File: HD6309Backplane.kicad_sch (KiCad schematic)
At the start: 8 parts, among them J1 Conn_01x02_Female, J2 Conn_02x30_Odd_Even, J3 Conn_01x02_Female, J4 Conn_01x02_Female, J5 Conn_01x02_Female, J6 Conn_02x30_Odd_Even, J7 Conn_02x30_Odd_Even, J8 Conn_02x30_Odd_Even

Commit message: align to new expansion position
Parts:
- added J10: Power probe, Connector_PinSocket_2.54mm:PinSocket_1x02_P2.54mm_Vertical, symbol Connector:Conn_01x02_Female
- added J9: External power, Connector_PinSocket_2.54mm:PinSocket_1x02_P2.54mm_Vertical, symbol Connector:Conn_01x02_Female
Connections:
- net +5V: now also J10.1 (Pin_1), J9.1 (Pin_1)
- net GND: now also J10.2 (Pin_2), J9.2 (Pin_2)
- net Q8: now reaches J7.45 (Pin_45)
- net Q8: now also J2.45 (Pin_45), J6.45 (Pin_45), J8.45 (Pin_45)
- no-connect marks 36 -> 32
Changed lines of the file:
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@@
   (no_connect (at 39.116 156.21))
   (no_connect (at 26.416 143.51))
-  (no_connect (at 192.024 52.07))
-  (no_connect (at 36.576 143.51))
   (no_connect (at 27.178 96.266))
   (no_connect (at 29.718 47.498))
@@
   (no_connect (at 100.838 47.498))
   (no_connect (at 176.784 52.07))
-  (no_connect (at 44.958 47.498))
   (no_connect (at 60.198 96.266))
   (no_connect (at 59.436 143.51))
-  (no_connect (at 37.338 96.266))
   (no_connect (at 93.218 96.266))
   (no_connect (at 21.336 143.51))
@@
     )
   )
+  (global_label "Q8" (shape input) (at 36.576 143.51 90) (fields_autoplaced)
+    (effects (font (size 1.27 1.27)) (justify left))
+    (property "Intersheet References" "${INTERSHEET_REFS}" (id 0) (at 36.4966 138.5569 90)
+      (effects (font (size 1.27 1.27)) (justify left) hide)
+    )
+  )
+  (global_label "Q8" (shape input) (at 44.958 47.498 90) (fields_autoplaced)
+    (effects (font (size 1.27 1.27)) (justify left))
+    (property "Intersheet References" "${INTERSHEET_REFS}" (id 0) (at 44.8786 42.5449 90)
+      (effects (font (size 1.27 1.27)) (justify left) hide)
+    )
+  )
   (global_label "Clock24" (shape input) (at 90.678 96.266 90) (fields_autoplaced)
     (effects (font (size 1.27 1.27)) (justify left))
@@
     )
   )
+  (global_label "Q8" (shape input) (at 192.024 52.07 90) (fields_autoplaced)
+    (effects (font (size 1.27 1.27)) (justify left))
+    (property "Intersheet References" "${INTERSHEET_REFS}" (id 0) (at 191.9446 47.1169 90)
+      (effects (font (size 1.27 1.27)) (justify left) hide)
+    )
+  )
   (global_label "~{Q}" (shape input) (at 82.296 143.51 90) (fields_autoplaced)
     (effects (font (size 1.27 1.27)) (justify left))
@@
     (effects (font (size 1.27 1.27)) (justify left))
     (property "Intersheet References" "${INTERSHEET_REFS}" (id 0) (at 80.5974 42.6054 90)
+      (effects (font (size 1.27 1.27)) (justify left) hide)
+    )
+  )
+  (global_label "Q8" (shape input) (at 37.338 96.266 90) (fields_autoplaced)
+    (effects (font (size 1.27 1.27)) (justify left))
+    (property "Intersheet References" "${INTERSHEET_REFS}" (id 0) (at 37.2586 91.3129 90)
       (effects (font (size 1.27 1.27)) (justify left) hide)
     )
@@
     )
     (property "Datasheet" "" (id 3) (at 83.82 29.972 0)
+      (effects (font (size 1.27 1.27)) hide)
+    )
+    (pin "1")
+  )
+  (symbol (lib_id "power:+5V") (at 155.956 120.142 0) (unit 1)
+    (in_bom yes) (on_board yes) (fields_autoplaced)
+    (property "Reference" "#PWR019" (id 0) (at 155.956 123.952 0)
+      (effects (font (size 1.27 1.27)) hide)
+    )
+    (property "Value" "+5V" (id 1) (at 155.956 115.316 0))
+    (property "Footprint" "" (id 2) (at 155.956 120.142 0)
+      (effects (font (size 1.27 1.27)) hide)
+    )
+    (property "Datasheet" "" (id 3) (at 155.956 120.142 0)
       (effects (font (size 1.27 1.27)) hide)
     )
@@
     (pin "9")
   )
+  (symbol (lib_id "power:GND") (at 155.956 122.682 0) (unit 1)
+    (in_bom yes) (on_board yes) (fields_autoplaced)
+    (property "Reference" "#PWR020" (id 0) (at 155.956 129.032 0)
+      (effects (font (size 1.27 1.27)) hide)
+    )
+    (property "Value" "GND" (id 1) (at 155.956 127.254 0))
+    (property "Footprint" "" (id 2) (at 155.956 122.682 0)
+      (effects (font (size 1.27 1.27)) hide)
+    )
+    (property "Datasheet" "" (id 3) (at 155.956 122.682 0)
+      (effects (font (size 1.27 1.27)) hide)
+    )
+    (pin "1")
+  )
   (symbol (lib_id "Connector:Conn_01x02_Female") (at 242.57 31.496 0) (unit 1)
     (in_bom yes) (on_board yes) (fields_autoplaced)
@@
     (pin "2")
   )
+  (symbol (lib_id "power:+5V") (at 155.702 103.886 0) (unit 1)
+    (in_bom yes) (on_board yes) (fields_autoplaced)
+    (property "Reference" "#PWR016" (id 0) (at 155.702 107.696 0)
+      (effects (font (size 1.27 1.27)) hide)
+    )
+    (property "Value" "+5V" (id 1) (at 155.702 99.06 0))
+    (property "Footprint" "" (id 2) (at 155.702 103.886 0)
+      (effects (font (size 1.27 1.27)) hide)
+    )
+    (property "Datasheet" "" (id 3) (at 155.702 103.886 0)
+      (effects (font (size 1.27 1.27)) hide)
+    )
+    (pin "1")
+  )
   (symbol (lib_id "power:GND") (at 177.546 35.306 0) (unit 1)
     (in_bom yes) (on_board yes) (fields_autoplaced)
@@
     )
     (pin "1")
+  )
+  (symbol (lib_id "power:GND") (at 155.702 106.426 0) (unit 1)
+    (in_bom yes) (on_board yes) (fields_autoplaced)
+    (property "Reference" "#PWR017" (id 0) (at 155.702 112.776 0)
+      (effects (font (size 1.27 1.27)) hide)
+    )
+    (property "Value" "GND" (id 1) (at 155.702 110.998 0))
+    (property "Footprint" "" (id 2) (at 155.702 106.426 0)
+      (effects (font (size 1.27 1.27)) hide)
+    )
+    (property "Datasheet" "" (id 3) (at 155.702 106.426 0)
+      (effects (font (size 1.27 1.27)) hide)
+    )
+    (pin "1")
+  )
+  (symbol (lib_id "Connector:Conn_01x02_Female") (at 160.782 103.886 0) (unit 1)
+    (in_bom yes) (on_board yes) (fields_autoplaced)
+    (property "Reference" "J9" (id 0) (at 161.544 103.8859 0)
+      (effects (font (size 1.27 1.27)) (justify left))
+    )
+    (property "Value" "External power" (id 1) (at 161.544 106.4259 0)
+      (effects (font (size 1.27 1.27)) (justify left))
+    )
+    (property "Footprint" "Connector_PinSocket_2.54mm:PinSocket_1x02_P2.54mm_Vertical" (id 2) (at 160.782 103.886 0)
+      (effects (font (size 1.27 1.27)) hide)
+    )
+    (property "Datasheet" "~" (id 3) (at 160.782 103.886 0)
+      (effects (font (size 1.27 1.27)) hide)
+    )
+    (pin "1")
+    (pin "2")
   )
   (symbol (lib_id "Connector_Generic:Conn_02x30_Odd_Even") (at 56.896 148.59 270) (unit 1)
@@
     (pin "1")
   )
+  (symbol (lib_id "Connector:Conn_01x02_Female") (at 161.036 120.142 0) (unit 1)
+    (in_bom yes) (on_board yes) (fields_autoplaced)
+    (property "Reference" "J10" (id 0) (at 161.798 120.1419 0)
+      (effects (font (size 1.27 1.27)) (justify left))
+    )
+    (property "Value" "Power probe" (id 1) (at 161.798 122.6819 0)
+      (effects (font (size 1.27 1.27)) (justify left))
+    )
+    (property "Footprint" "Connector_PinSocket_2.54mm:PinSocket_1x02_P2.54mm_Vertical" (id 2) (at 161.036 120.142 0)
+      (effects (font (size 1.27 1.27)) hide)
+    )
+    (property "Datasheet" "~" (id 3) (at 161.036 120.142 0)
+      (effects (font (size 1.27 1.27)) hide)
+    )
+    (pin "1")
+    (pin "2")
+  )
   (symbol (lib_id "power:+5V") (at 83.82 27.432 0) (unit 1)
     (in_bom yes) (on_board yes) (fields_autoplaced)
@@
       (reference "#PWR015") (unit 1) (value "+5V") (footprint "")
     )
+    (path "/8b947d1a-ce20-4218-9a3c-63eecca4c075"
+      (reference "#PWR016") (unit 1) (value "+5V") (footprint "")
+    )
+    (path "/b3f889d3-c00c-4e39-8b1d-e37941cea040"
+      (reference "#PWR017") (unit 1) (value "GND") (footprint "")
+    )
     (path "/04b6a0a1-8ff0-4daa-918c-930663744d50"
       (reference "#PWR018") (unit 1) (value "+5V") (footprint "")
     )
+    (path "/2037523f-8ef9-4ff2-a248-01a9f31a3eb5"
+      (reference "#PWR019") (unit 1) (value "+5V") (footprint "")
+    )
+    (path "/825dee91-fb4b-4957-9524-3022f9b93baf"
+      (reference "#PWR020") (unit 1) (value "GND") (footprint "")
+    )
     (path "/3992ff7e-16e7-40cc-9fb3-3ae7d9eb5f3a"
       (reference "J1") (unit 1) (value "Conn_01x02_Female") (footprint "Connector_PinSocket_2.54mm:PinSocket_1x02_P2.54mm_Vertical")
@@
       (reference "J8") (unit 1) (value "Conn_02x30_Odd_Even") (footprint "Connector_PinSocket_2.54mm:PinSocket_2x30_P2.54mm_Vertical")
     )
-  )
+    (path "/bac68116-967b-4b60-a3ef-e7e9a8644fbb"
+      (reference "J9") (unit 1) (value "External power") (footprint "Connector_PinSocket_2.54mm:PinSocket_1x02_P2.54mm_Vertical")
+    )
+    (path "/da05af8c-bcc2-4152-b839-cc8e4505fae5"
+      (reference "J10") (unit 1) (value "Power probe") (footprint "Connector_PinSocket_2.54mm:PinSocket_1x02_P2.54mm_Vertical")
+    )
+  )

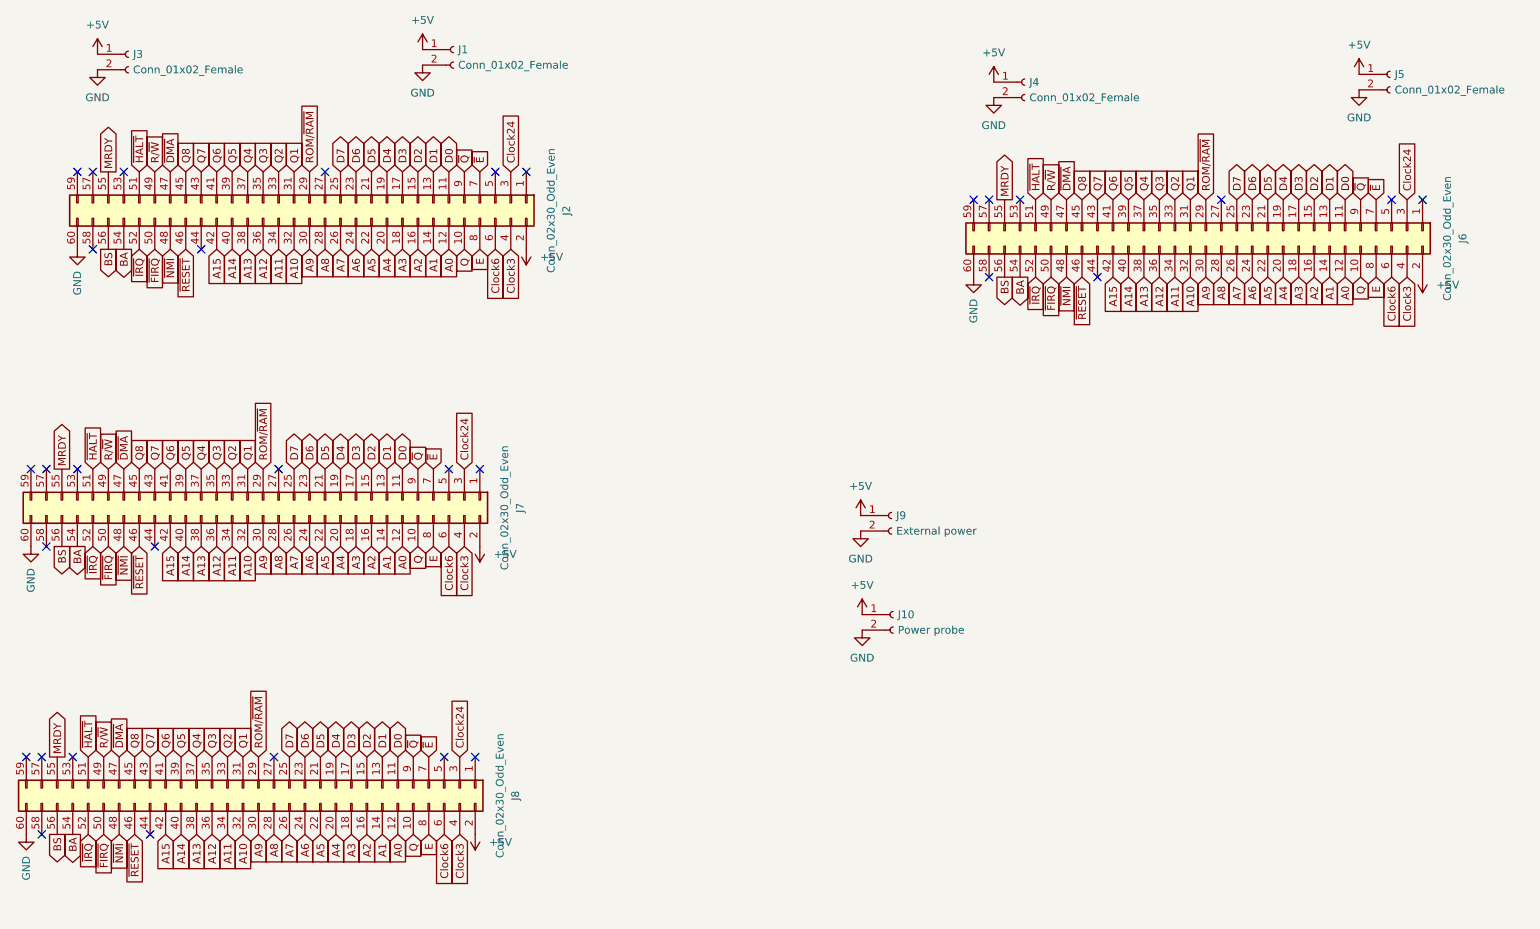
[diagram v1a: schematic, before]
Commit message: add mapped memory lane
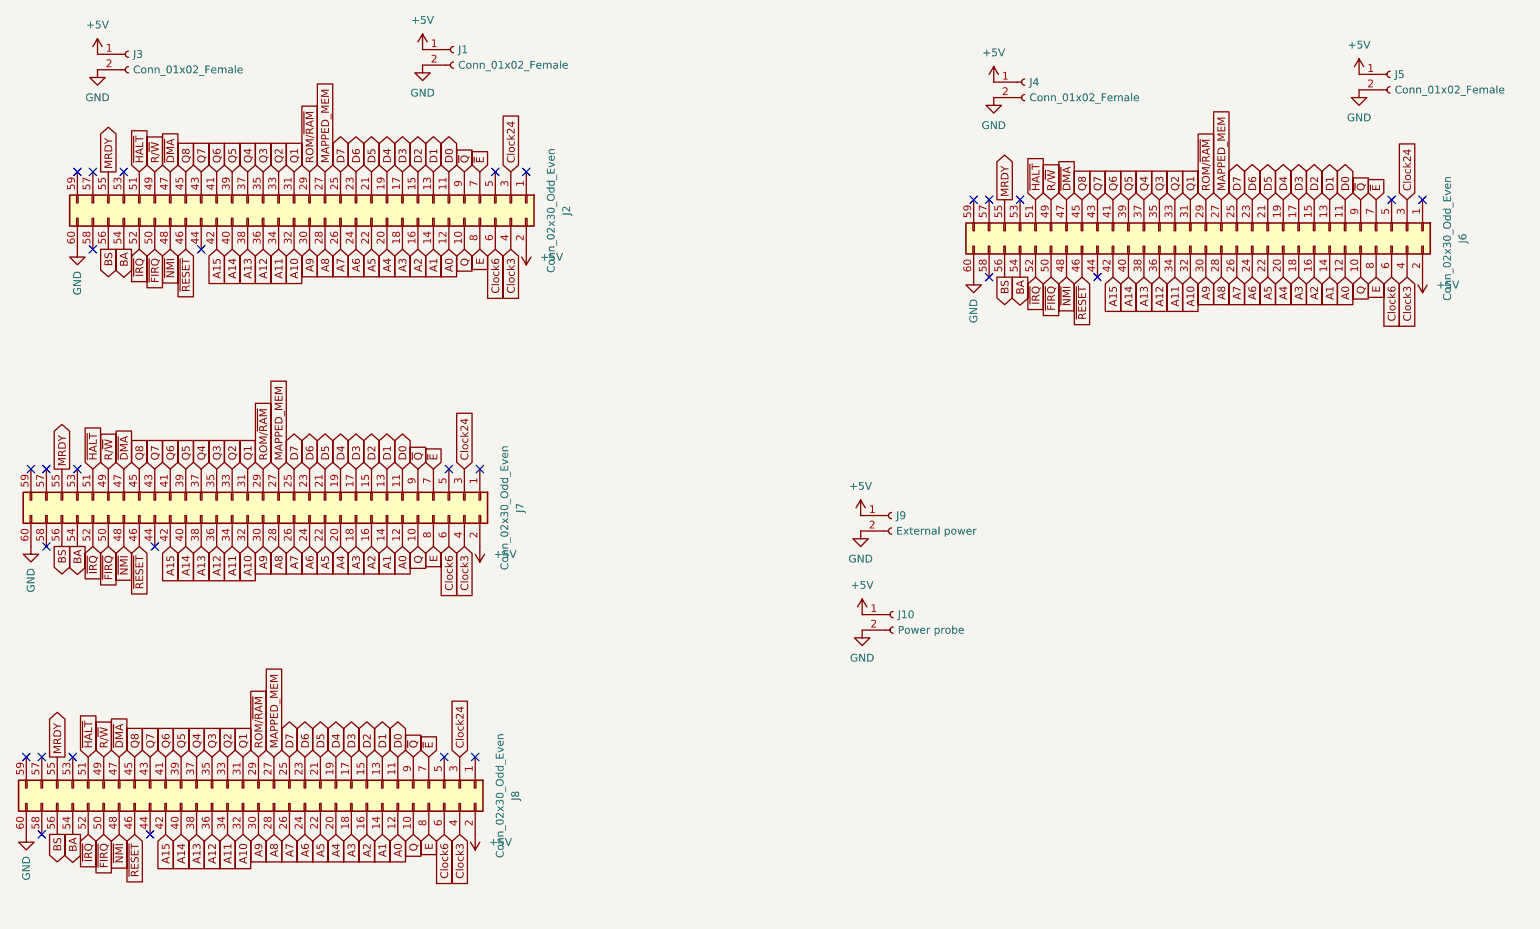
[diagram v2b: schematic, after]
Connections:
- net MAPPED_MEM: now reaches J7.27 (Pin_27)
- net MAPPED_MEM: now also J2.27 (Pin_27), J6.27 (Pin_27), J8.27 (Pin_27)
- no-connect marks 32 -> 28
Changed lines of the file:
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@@
   (no_connect (at 92.456 143.51))
   (no_connect (at 176.784 64.77))
-  (no_connect (at 214.884 52.07))
   (no_connect (at 19.558 96.266))
   (no_connect (at 39.116 156.21))
@@
   (no_connect (at 29.718 47.498))
   (no_connect (at 22.098 108.966))
-  (no_connect (at 67.818 47.498))
   (no_connect (at 88.138 96.266))
   (no_connect (at 174.244 52.07))
   (no_connect (at 100.838 47.498))
   (no_connect (at 176.784 52.07))
-  (no_connect (at 60.198 96.266))
-  (no_connect (at 59.436 143.51))
   (no_connect (at 93.218 96.266))
   (no_connect (at 21.336 143.51))
@@
     )
   )
+  (global_label "MAPPED_MEM" (shape input) (at 214.884 52.07 90) (fields_autoplaced)
+    (effects (font (size 1.27 1.27)) (justify left))
+    (property "Intersheet References" "${INTERSHEET_REFS}" (id 0) (at 214.8046 37.1383 90)
+      (effects (font (size 1.27 1.27)) (justify left) hide)
+    )
+  )
   (global_label "A1" (shape input) (at 85.598 60.198 270) (fields_autoplaced)
     (effects (font (size 1.27 1.27)) (justify right))
@@
     )
   )
+  (global_label "MAPPED_MEM" (shape input) (at 59.436 143.51 90) (fields_autoplaced)
+    (effects (font (size 1.27 1.27)) (justify left))
+    (property "Intersheet References" "${INTERSHEET_REFS}" (id 0) (at 59.3566 128.5783 90)
+      (effects (font (size 1.27 1.27)) (justify left) hide)
+    )
+  )
   (global_label "A10" (shape input) (at 209.804 64.77 270) (fields_autoplaced)
     (effects (font (size 1.27 1.27)) (justify right))
@@
     )
   )
+  (global_label "MAPPED_MEM" (shape input) (at 67.818 47.498 90) (fields_autoplaced)
+    (effects (font (size 1.27 1.27)) (justify left))
+    (property "Intersheet References" "${INTERSHEET_REFS}" (id 0) (at 67.7386 32.5663 90)
+      (effects (font (size 1.27 1.27)) (justify left) hide)
+    )
+  )
   (global_label "Q5" (shape input) (at 44.958 96.266 90) (fields_autoplaced)
     (effects (font (size 1.27 1.27)) (justify left))
@@
     )
   )
+  (global_label "MAPPED_MEM" (shape input) (at 60.198 96.266 90) (fields_autoplaced)
+    (effects (font (size 1.27 1.27)) (justify left))
+    (property "Intersheet References" "${INTERSHEET_REFS}" (id 0) (at 60.1186 81.3343 90)
+      (effects (font (size 1.27 1.27)) (justify left) hide)
+    )
+  )
